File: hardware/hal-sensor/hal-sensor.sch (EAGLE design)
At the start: 7 parts, among them IC1 DRV5023AJEDBZRQ1, Q1 BCX71SMD

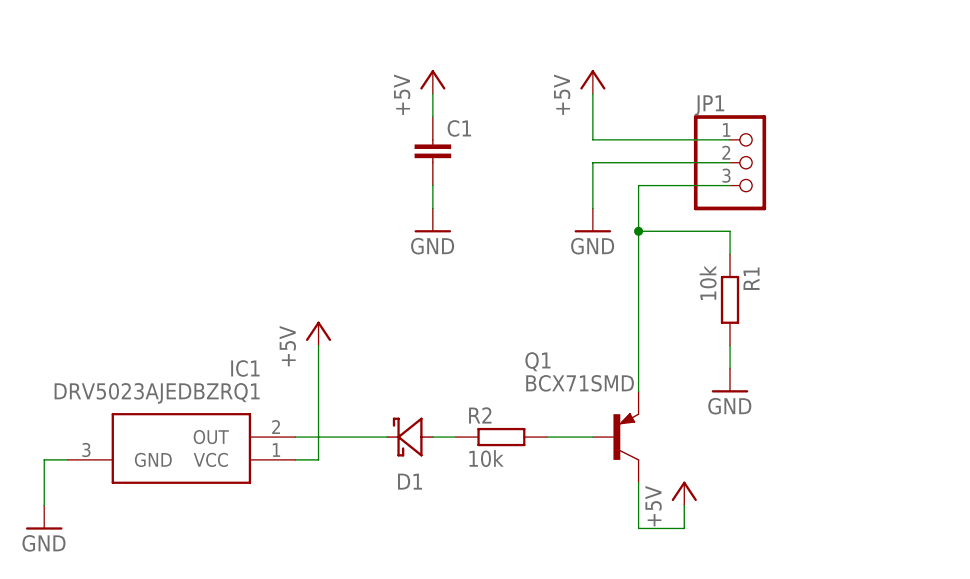
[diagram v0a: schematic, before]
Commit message: redo hall sensor board
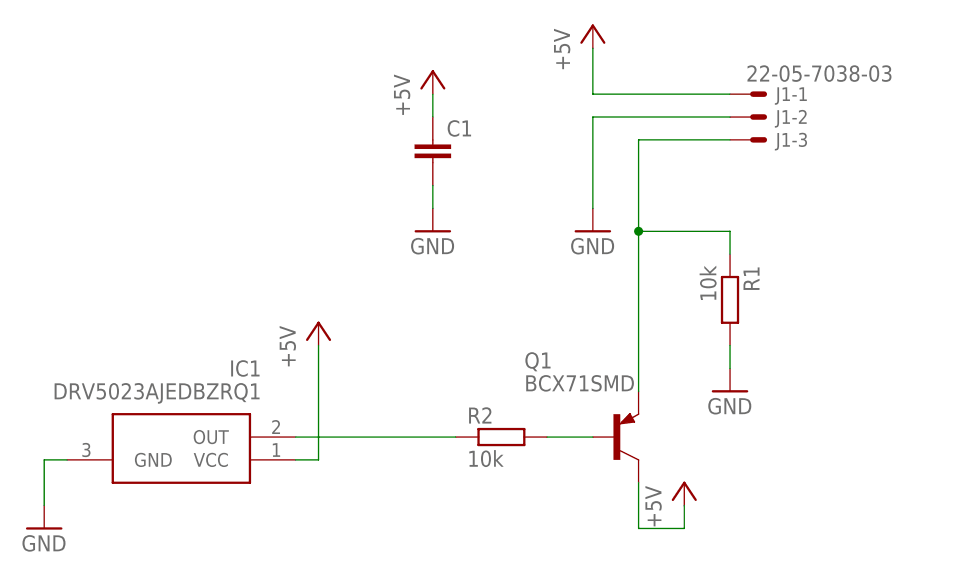
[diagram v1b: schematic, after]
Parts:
- removed D1: (no value), BeagleBone_Black_Wireless:GHI-BASICCOMPONENTS_DIODE-SCHOTTKY-(NXP)-SOD323-(REFLOW)
- removed JP1: (no value), pinhead:PINHD-1X3
- added J1: 22-05-7038-03, con-molex:22-05-7038-03
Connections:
- removed net N$2: D1.ANODE, R2.1
- net +5V: now also J1-1.S; no longer JP1.1
- net CTRL: now also J1-3.S; no longer JP1.3
- net GND: now also J1-2.S; no longer JP1.2
- net N$1: now also R2.1; no longer D1.CATHODE
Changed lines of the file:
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@@
 <part name="R1" library="resistor" library_urn="urn:adsk.eagle:library:348" deviceset="R-EU_" device="R0805" package3d_urn="urn:adsk.eagle:package:23553/2" value="10k"/>
 <part name="GND2" library="supply1" library_urn="urn:adsk.eagle:library:371" deviceset="GND" device=""/>
-<part name="JP1" library="pinhead" library_urn="urn:adsk.eagle:library:325" deviceset="PINHD-1X3" device="" package3d_urn="urn:adsk.eagle:package:22458/2"/>
 <part name="GND1" library="supply1" library_urn="urn:adsk.eagle:library:371" deviceset="GND" device=""/>
 <part name="P+2" library="supply1" library_urn="urn:adsk.eagle:library:371" deviceset="+5V" device=""/>
@@
 <part name="P+4" library="supply1" library_urn="urn:adsk.eagle:library:371" deviceset="+5V" device=""/>
 <part name="GND4" library="supply1" library_urn="urn:adsk.eagle:library:371" deviceset="GND" device=""/>
-<part name="D1" library="BeagleBone_Black_Wireless" library_urn="urn:adsk.eagle:library:6644236" deviceset="GHI-BASICCOMPONENTS_DIODE-SCHOTTKY-(NXP)-" device="SOD323-(REFLOW)" package3d_urn="urn:adsk.eagle:package:6644354/2"/>
 <part name="R2" library="resistor" library_urn="urn:adsk.eagle:library:348" deviceset="R-EU_" device="R0805" package3d_urn="urn:adsk.eagle:package:23553/2" value="10k"/>
 <part name="FRAME1" library="frames" library_urn="urn:adsk.eagle:library:229" deviceset="A4L-LOC" device=""/>
+<part name="J1" library="con-molex" library_urn="urn:adsk.eagle:library:165" deviceset="22-?-03" device="05-7038"/>
 </parts>
 <sheets>
@@
 <attribute name="VALUE" x="93.98" y="116.84" size="1.778" layer="96"/>
 </instance>
-<instance part="JP1" gate="A" x="99.06" y="144.78" smashed="yes">
-<attribute name="NAME" x="92.71" y="150.495" size="1.778" layer="95"/>
-<attribute name="VALUE" x="92.71" y="137.16" size="1.778" layer="96"/>
-</instance>
 <instance part="GND1" gate="1" x="81.28" y="137.16" smashed="yes">
 <attribute name="VALUE" x="78.74" y="134.62" size="1.778" layer="96"/>
 </instance>
-<instance part="P+2" gate="1" x="81.28" y="154.94" smashed="yes">
-<attribute name="VALUE" x="78.74" y="149.86" size="1.778" layer="96" rot="R90"/>
+<instance part="P+2" gate="1" x="81.28" y="160.02" smashed="yes">
+<attribute name="VALUE" x="78.74" y="154.94" size="1.778" layer="96" rot="R90"/>
 </instance>
 <instance part="IC1" gate="G$1" x="48.26" y="111.76" smashed="yes" rot="R180">
@@
 <attribute name="VALUE" x="60.96" y="134.62" size="1.778" layer="96"/>
 </instance>
-<instance part="D1" gate="G$1" x="60.96" y="114.3" smashed="yes" rot="R180">
-<attribute name="NAME" x="60.96" y="110.236" size="1.778" layer="95" rot="R180" align="bottom-center"/>
-<attribute name="VALUE" x="60.96" y="118.618" size="1.778" layer="96" rot="R180" align="top-center"/>
-</instance>
 <instance part="R2" gate="G$1" x="71.12" y="114.3" smashed="yes">
 <attribute name="NAME" x="67.31" y="115.7986" size="1.778" layer="95"/>
@@
 <attribute name="LAST_DATE_TIME" x="217.17" y="10.16" size="2.286" layer="94"/>
 <attribute name="SHEET" x="230.505" y="5.08" size="2.54" layer="94"/>
+</instance>
+<instance part="J1" gate="-1" x="99.06" y="152.4" smashed="yes">
+<attribute name="NAME" x="101.6" y="151.638" size="1.524" layer="95"/>
+<attribute name="VALUE" x="98.298" y="153.797" size="1.778" layer="96"/>
+</instance>
+<instance part="J1" gate="-2" x="99.06" y="149.86" smashed="yes">
+<attribute name="NAME" x="101.6" y="149.098" size="1.524" layer="95"/>
+</instance>
+<instance part="J1" gate="-3" x="99.06" y="147.32" smashed="yes">
+<attribute name="NAME" x="101.6" y="146.558" size="1.524" layer="95"/>
 </instance>
 </instances>
@@
 </segment>
 <segment>
-<pinref part="JP1" gate="A" pin="1"/>
-<wire x1="96.52" y1="147.32" x2="81.28" y2="147.32" width="0.1524" layer="91"/>
-<wire x1="81.28" y1="147.32" x2="81.28" y2="152.4" width="0.1524" layer="91"/>
+<wire x1="96.52" y1="152.4" x2="81.28" y2="152.4" width="0.1524" layer="91"/>
+<wire x1="81.28" y1="152.4" x2="81.28" y2="157.48" width="0.1524" layer="91"/>
 <pinref part="P+2" gate="1" pin="+5V"/>
+<pinref part="J1" gate="-1" pin="S"/>
 </segment>
 <segment>
@@
 <wire x1="86.36" y1="119.38" x2="86.36" y2="137.16" width="0.1524" layer="91"/>
 <pinref part="R1" gate="G$1" pin="1"/>
-<wire x1="86.36" y1="137.16" x2="86.36" y2="142.24" width="0.1524" layer="91"/>
 <junction x="86.36" y="137.16"/>
-<pinref part="JP1" gate="A" pin="3"/>
-<wire x1="86.36" y1="142.24" x2="96.52" y2="142.24" width="0.1524" layer="91"/>
 <wire x1="96.52" y1="134.62" x2="96.52" y2="137.16" width="0.1524" layer="91"/>
 <wire x1="96.52" y1="137.16" x2="86.36" y2="137.16" width="0.1524" layer="91"/>
+<pinref part="J1" gate="-3" pin="S"/>
+<wire x1="96.52" y1="147.32" x2="86.36" y2="147.32" width="0.1524" layer="91"/>
+<wire x1="86.36" y1="147.32" x2="86.36" y2="137.16" width="0.1524" layer="91"/>
 </segment>
 </net>
@@
 </segment>
 <segment>
-<pinref part="JP1" gate="A" pin="2"/>
-<wire x1="96.52" y1="144.78" x2="81.28" y2="144.78" width="0.1524" layer="91"/>
-<wire x1="81.28" y1="144.78" x2="81.28" y2="139.7" width="0.1524" layer="91"/>
+<wire x1="96.52" y1="149.86" x2="81.28" y2="149.86" width="0.1524" layer="91"/>
+<wire x1="81.28" y1="149.86" x2="81.28" y2="139.7" width="0.1524" layer="91"/>
 <pinref part="GND1" gate="1" pin="GND"/>
+<pinref part="J1" gate="-2" pin="S"/>
 </segment>
 <segment>
@@
 <segment>
 <pinref part="IC1" gate="G$1" pin="OUT"/>
-<pinref part="D1" gate="G$1" pin="CATHODE"/>
-<wire x1="48.26" y1="114.3" x2="58.42" y2="114.3" width="0.1524" layer="91"/>
+<wire x1="48.26" y1="114.3" x2="66.04" y2="114.3" width="0.1524" layer="91"/>
+<pinref part="R2" gate="G$1" pin="1"/>
 </segment>
 </net>
-<net name="N$2" class="0">
-<segment>
-<pinref part="D1" gate="G$1" pin="ANODE"/>
-<pinref part="R2" gate="G$1" pin="1"/>
-<wire x1="63.5" y1="114.3" x2="66.04" y2="114.3" width="0.1524" layer="91"/>
-</segment>
-</net>
